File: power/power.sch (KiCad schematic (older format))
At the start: 62 parts, among them M1 HIP2101, M2 HIP2101, M3 HIP2101, M4 ACS722, M5 ACS722, P1 PLS_10, P3 C, P4 A, P5 B, P6 VDD, P7 GND, P8 PLS_3, P9 PLS_3, Q1 CSD18532, Q2 CSD18532, Q3 CSD18532, Q4 CSD18532, Q5 CSD18532, Q6 CSD18532

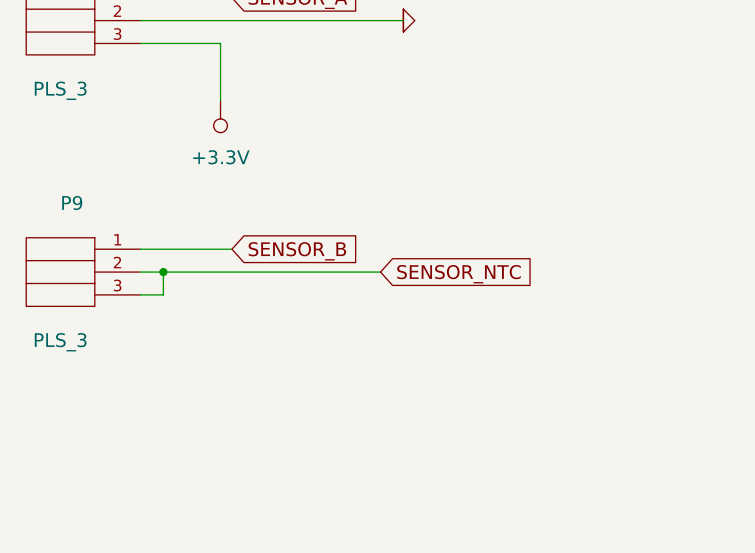
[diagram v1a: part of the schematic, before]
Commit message: Added OpAmp buffer, a lot of small fixes.
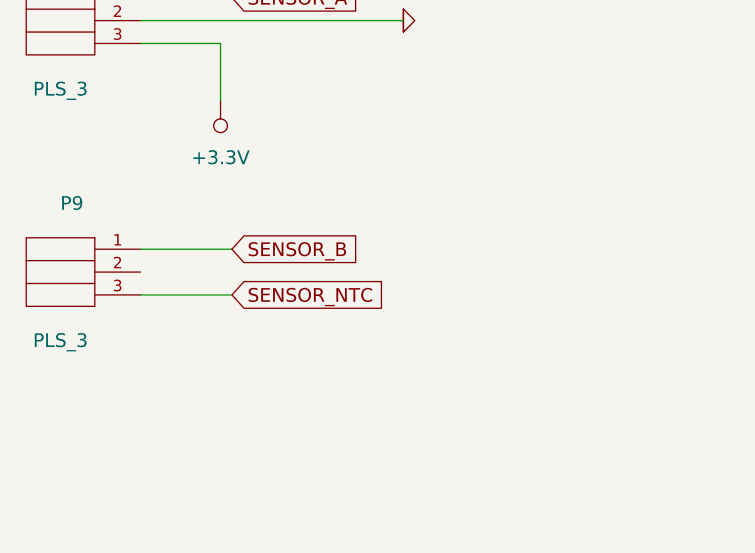
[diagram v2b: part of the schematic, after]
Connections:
- net SENSOR_NTC: no longer P9.2
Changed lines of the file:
@@
 Wire Wire Line
 	1800 7100 2950 7100
-Text GLabel 2850 8200 2    60   Input ~ 0
+Text GLabel 2200 8300 2    60   Input ~ 0
 SENSOR_NTC
-Wire Wire Line
-	2850 8200 1800 8200
 Text GLabel 7700 8600 2    60   Input ~ 0
 SENSOR_NTC
@@
 Connection ~ 7450 9100
 Wire Wire Line
-	1800 8300 1900 8300
-Wire Wire Line
-	1900 8300 1900 8200
-Connection ~ 1900 8200
+	2200 8300 1800 8300
 $EndSCHEMATC

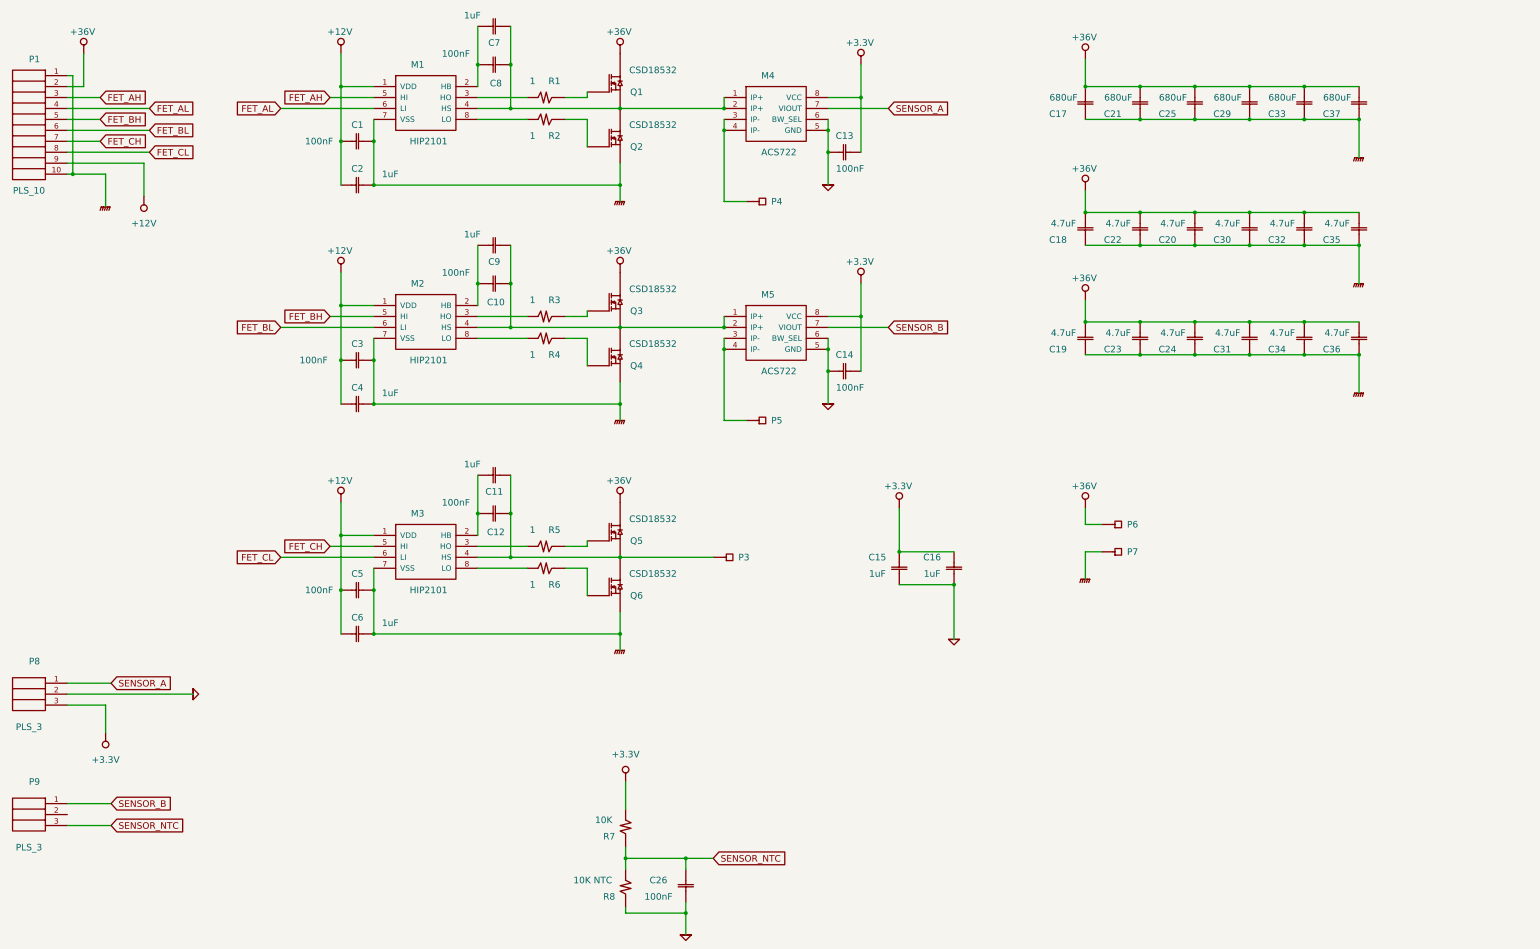
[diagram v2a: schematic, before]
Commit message: Accumulated changes, large track width, encoder/hall interface, etc.
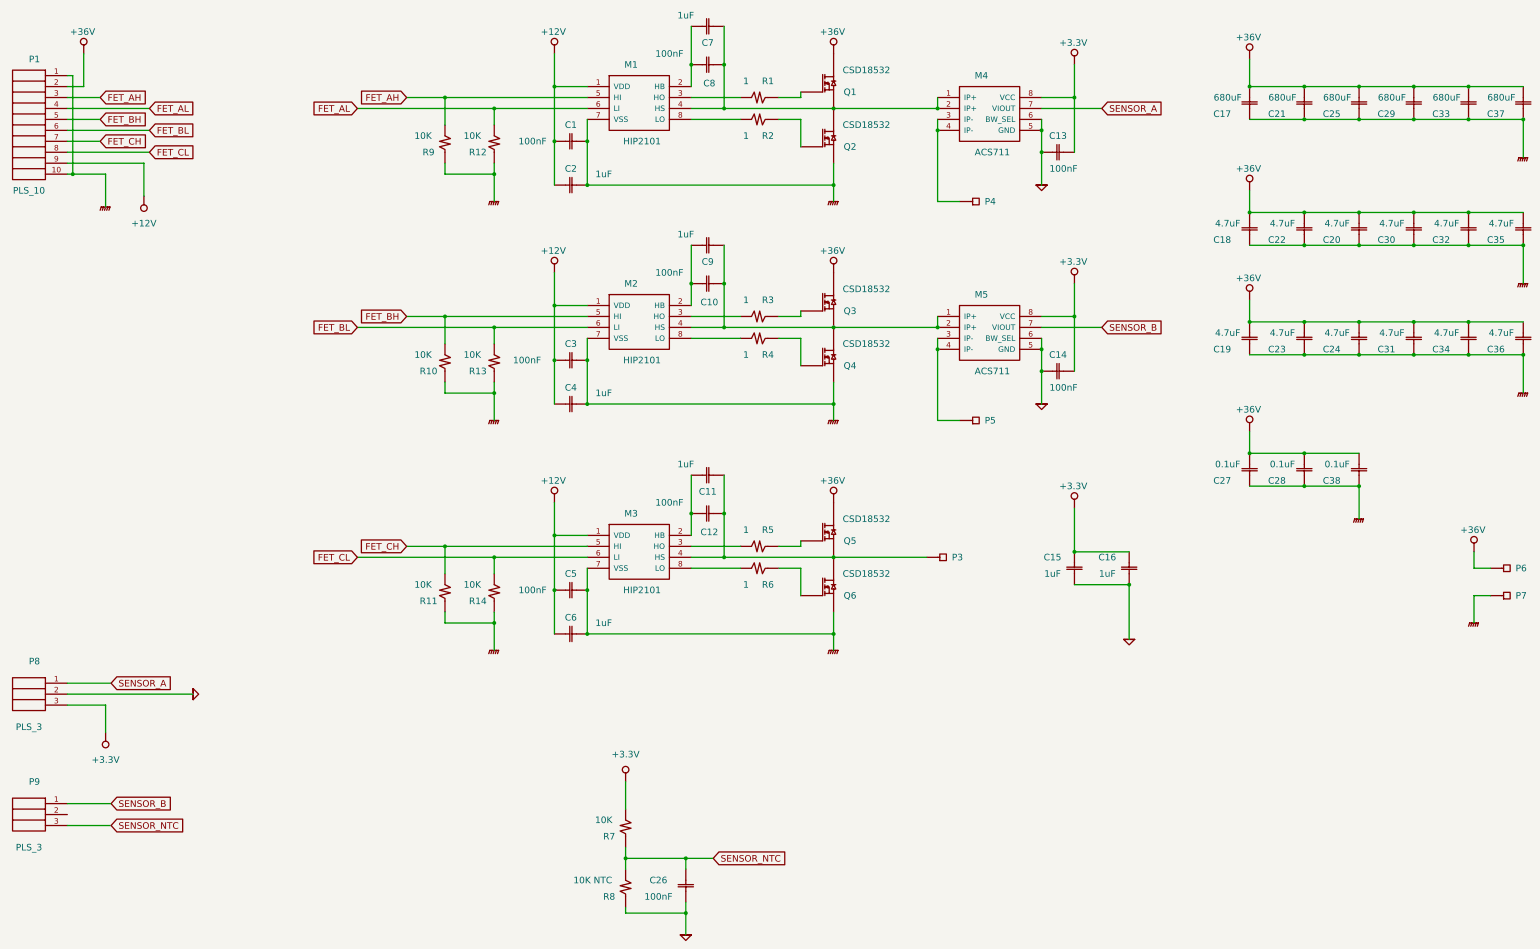
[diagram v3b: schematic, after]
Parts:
- added C27, C28, C38: 0.1uF, foot:SM0805, symbol C
- added R10, R11, R12, R13, R14, R9: 10K, foot:SM0603, symbol R
- M4, M5: value ACS722 -> ACS711
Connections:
- net +36V: now also C27.1, C28.1, C38.1
- net FET_AH: now also R9.2
- net FET_AL: now also R12.2
- net FET_BH: now also R10.2
- net FET_BL: now also R13.2
- net FET_CH: now also R11.2
- net FET_CL: now also R14.2
- net PGND: now also C27.2, C28.2, C38.2, R10.1, R11.1, R12.1, R13.1, R14.1, R9.1
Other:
- moved on the sheet: C1, C10, C11, C12, C13, C14, C15, C16, C17, C18, C19, C2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

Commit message: Reduced decoupling capacitor bank like ESC, also added two row of pins, small fixes.
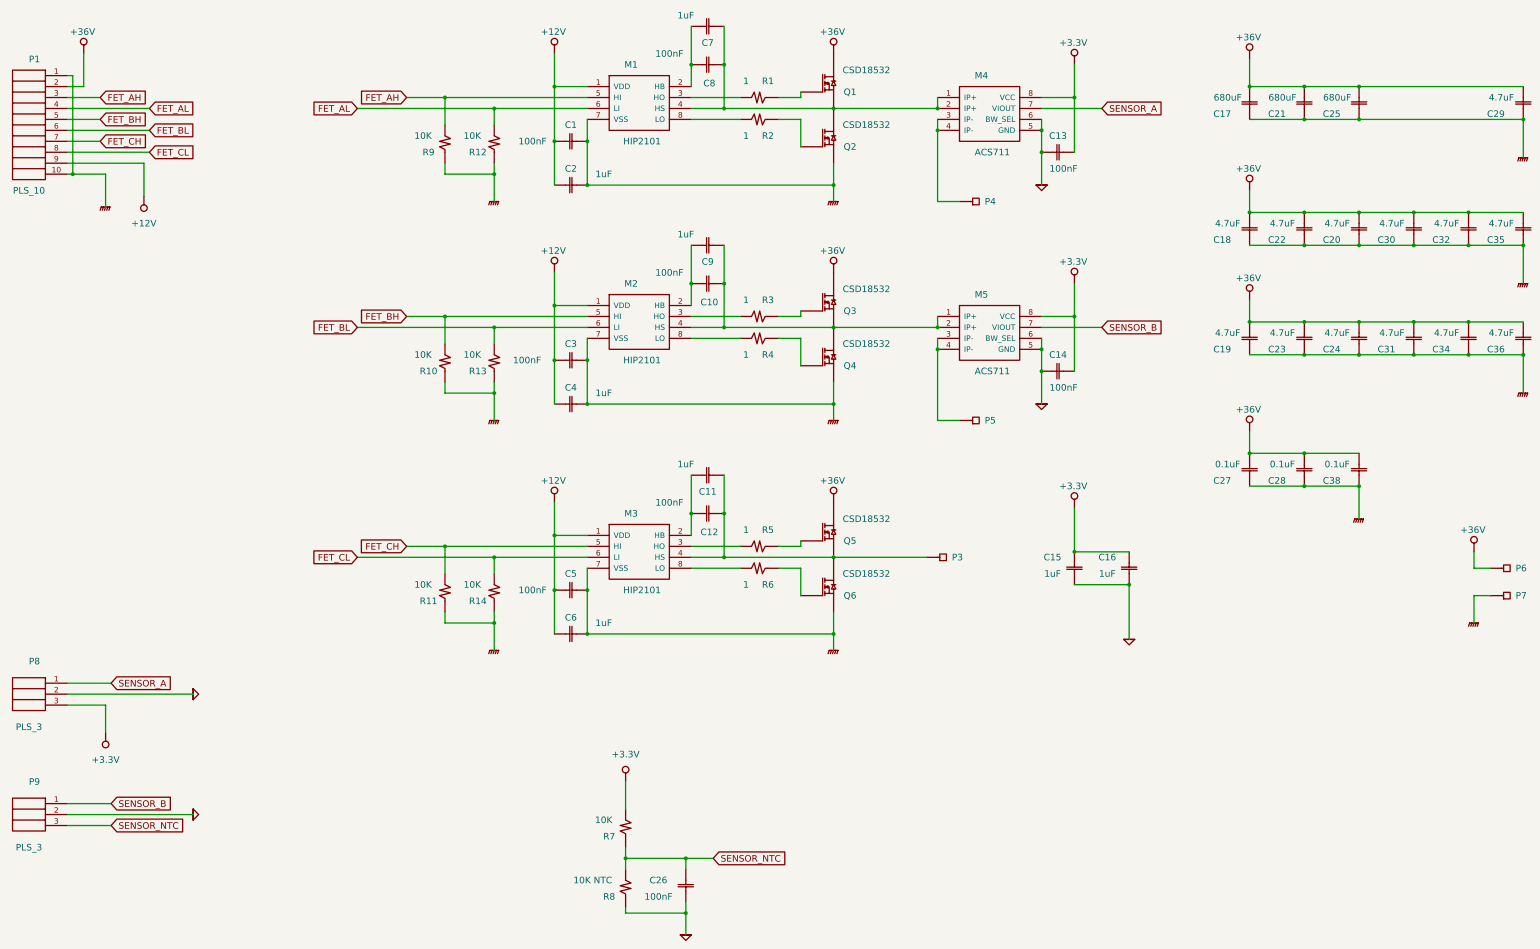
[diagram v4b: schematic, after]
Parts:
- removed C33, C37: 680uF, foot:CE135, symbol C
- C29: value 680uF -> 4.7uF; footprint foot:CE135 -> foot:SM2220
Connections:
- net AGND: now also P9.2

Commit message: Renew annotaion of power board, minor fixes.
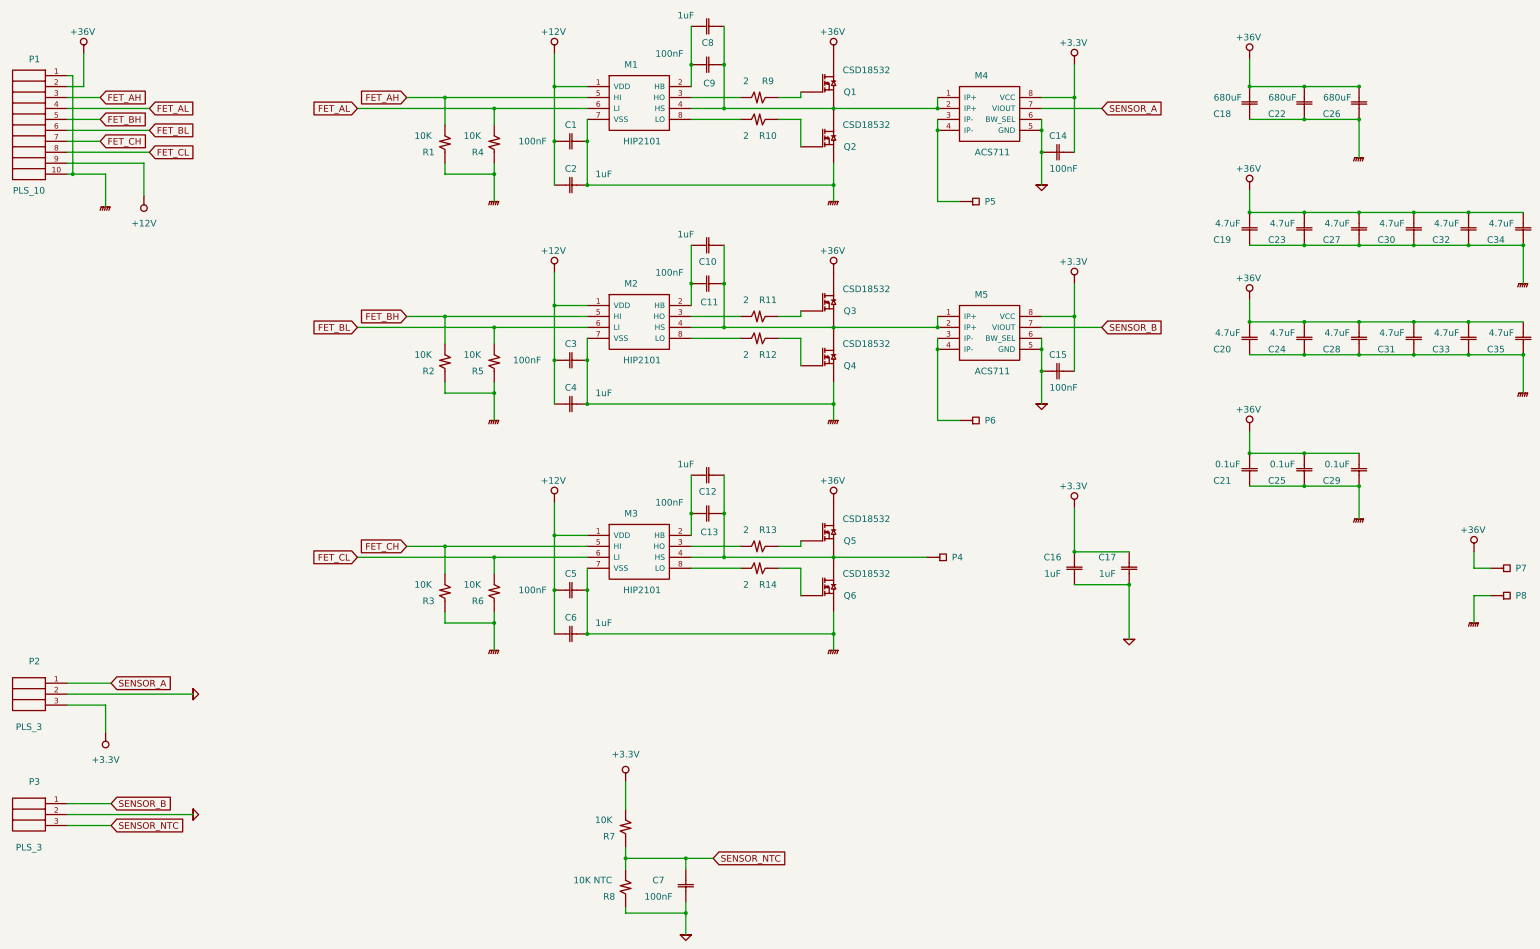
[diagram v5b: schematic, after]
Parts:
- removed C29: 4.7uF, foot:SM2220, symbol C
- C18: renamed from C17; footprint foot:CE135 -> foot:CE135L
- C22: renamed from C21; footprint foot:CE135 -> foot:CE135L
- C26: renamed from C25; footprint foot:CE135 -> foot:CE135L
- R10: renamed from R2; value 1 -> 2
- R11: renamed from R3; value 1 -> 2
- R12: renamed from R4; value 1 -> 2
- R13: renamed from R5; value 1 -> 2
- R14: renamed from R6; value 1 -> 2
- R9: renamed from R1; value 1 -> 2
- renumbered C9 to C10, C10 to C11, C11 to C12, C12 to C13, C13 to C14, C14 to C15, C15 to C16, C16 to C17, C18 to C19, C19 to C20, C27 to C21, C22 to C23, C23 to C24, C28 to C25, C20 to C27, C24 to C28, C38 to C29, C34 to C33, C35 to C34, C36 to C35, C26 to C7, C7 to C8, C8 to C9, P8 to P2, P9 to P3, P3 to P4, P4 to P5, P5 to P6, P6 to P7, P7 to P8, R9 to R1, R10 to R2, R11 to R3, R12 to R4, R13 to R5, R14 to R6

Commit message: Replaced ACS7XX sensors to the current shunt amplifiers.
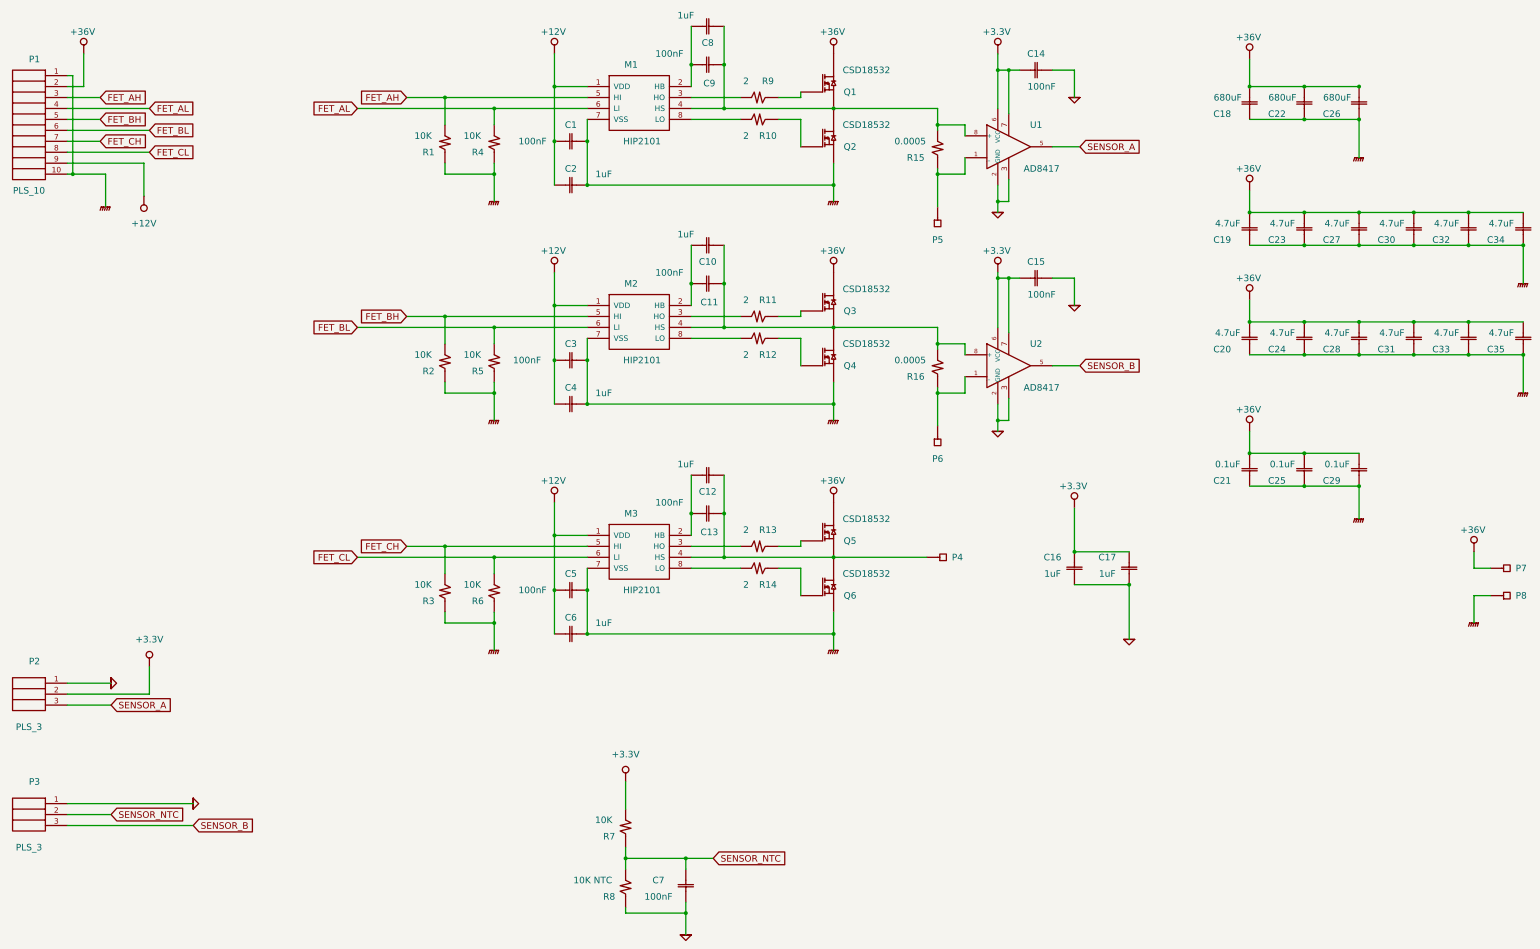
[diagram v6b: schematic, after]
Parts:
- removed M4, M5: ACS711, foot:SO8, symbol ACS722
- added R15, R16: 0.0005, foot:LR2512, symbol R
- added U1, U2: AD8417, foot:MSOP8, symbol AD8417
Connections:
- net +3.3V: now also C14.2, C15.2, P2.2, U1.6 (VCC), U1.7, U2.6 (VCC), U2.7; no longer C14.1, C15.1, P2.3
- net AGND: now also C14.1, C15.1, P2.1, P3.1, U1.2 (GND), U1.3, U2.2 (GND), U2.3; no longer C14.2, C15.2, P2.2, P3.2
- net SENSOR_A: now also P2.3, U1.5; no longer P2.1
- net SENSOR_B: now also P3.3, U2.5; no longer P3.1
- net SENSOR_NTC: now also P3.2; no longer P3.3
- net at C10.1, C11.1, M2.4 (HS)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: now also R16.2, U2.8 (+)
- net at P6.1: now also R16.1, U2.1 (_)
- net at C8.1, C9.1, M1.4 (HS)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: now also R15.2, U1.8 (+)
- net at P5.1: now also R15.1, U1.1 (_)
- new net NC: U1.4 (NC), U2.4 (NC)
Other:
- moved on the sheet: C14, C15, P5, P6

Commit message: Fixed a few small mistakes.
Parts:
- R7: value 10K -> 10K 1%
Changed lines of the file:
@@
 P 6900 8300
 F 0 "R7" V 7000 8150 60  0000 C CNN
-F 1 "10K" V 6850 8100 60  0000 C CNN
+F 1 "10K 1%" V 6850 8050 60  0000 C CNN
 F 2 "foot:SM0603" H 6900 8300 60  0001 C CNN
 F 3 "" H 6900 8300 60  0000 C CNN
